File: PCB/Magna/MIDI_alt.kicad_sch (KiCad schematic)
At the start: 32 parts, among them J501 DIN-5_180degree, J502 DIN-5_180degree, J503 DIN-5_180degree, U501 74LVC2G14, U502 74LVC2G14, U503 74HC08D, U504 TLP2361

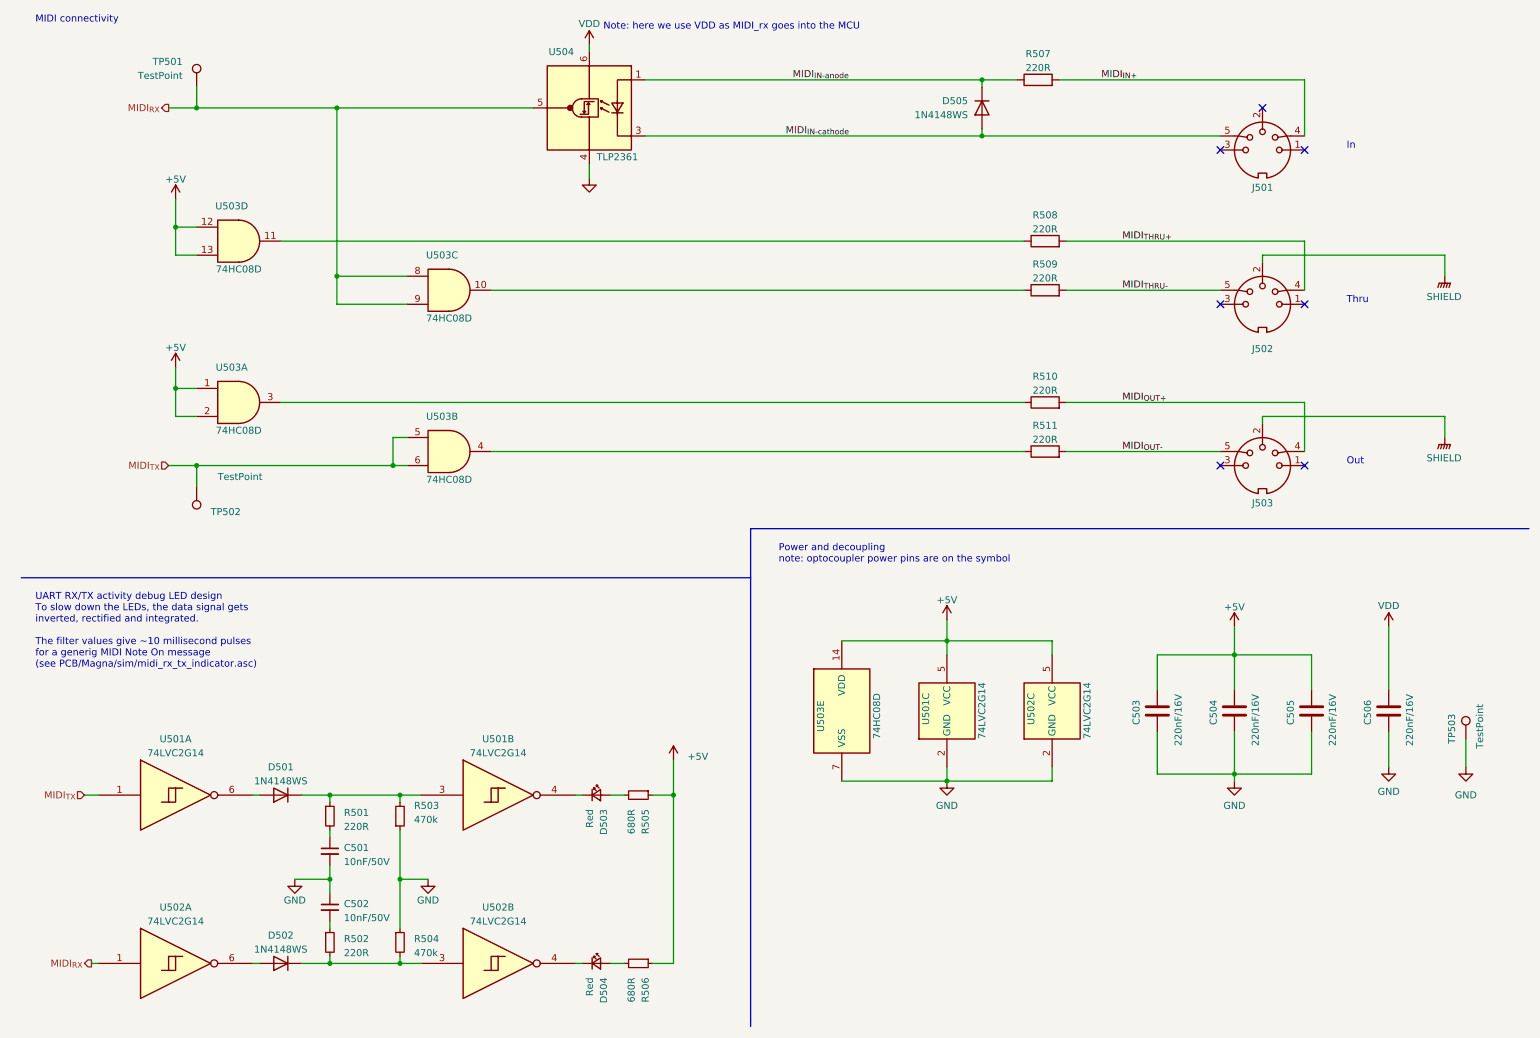
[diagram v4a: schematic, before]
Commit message: Update schematics to Kicad 9
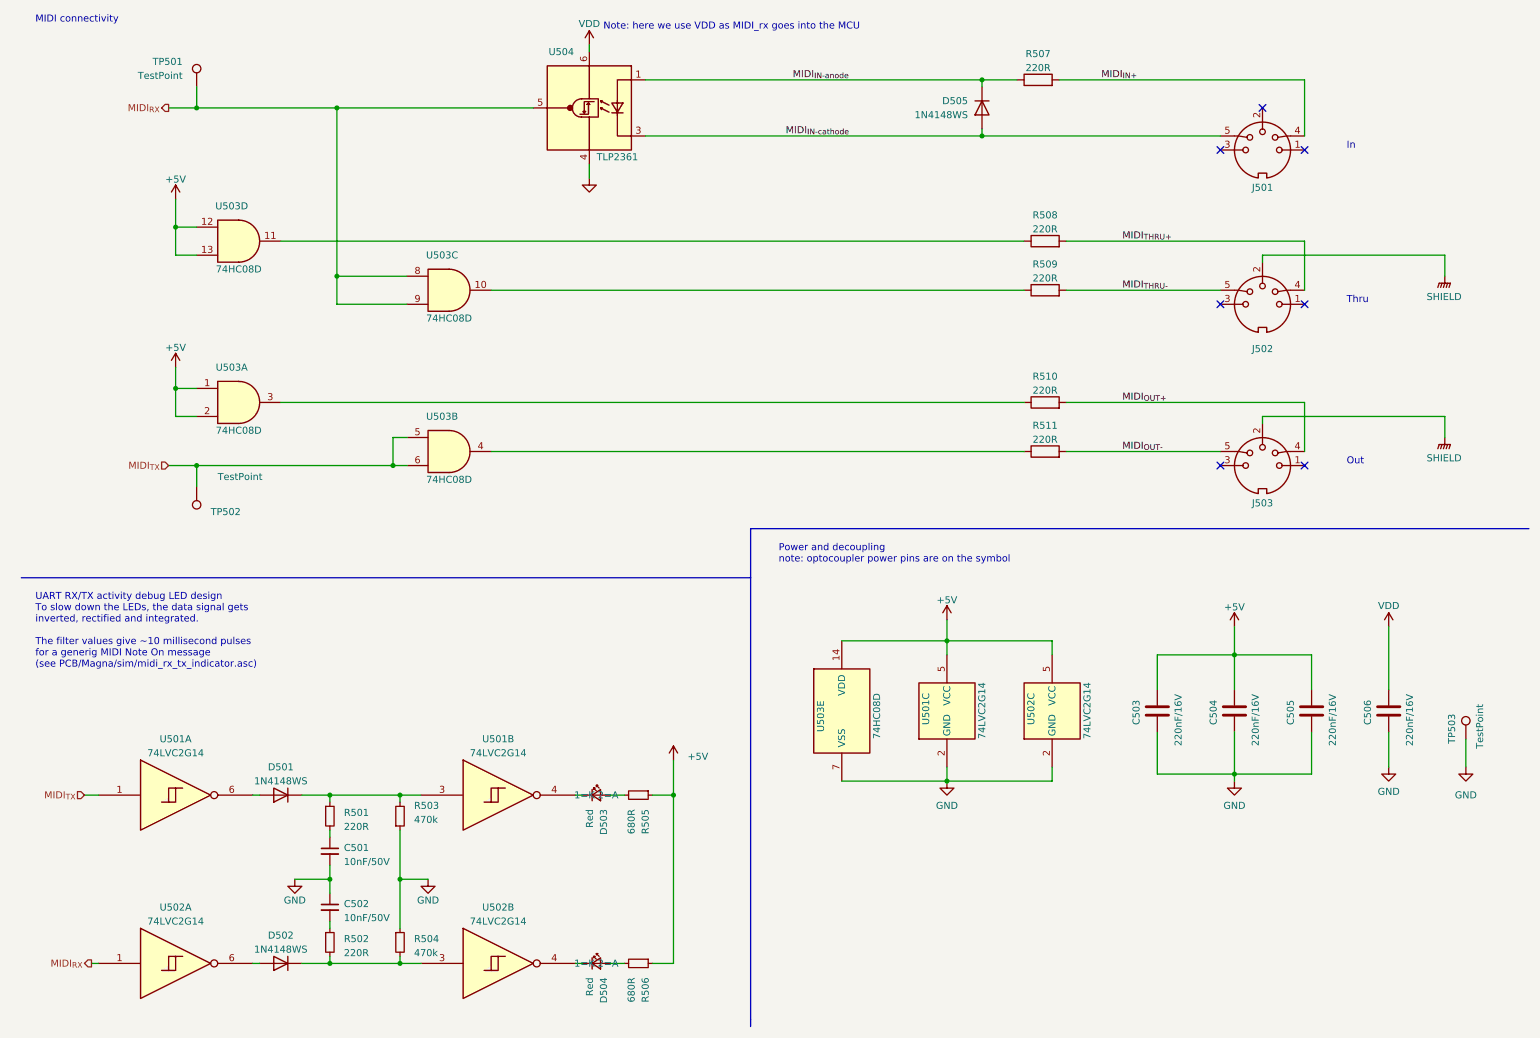
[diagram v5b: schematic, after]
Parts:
- D501, D502, D505: footprint Diode_SMD:D_SOD-123 -> Diode_SMD:D_SOD-523
- U504: footprint Package_SO:SO-5_4.4x3.6mm_P1.27mm -> Package_SO:SO-6L_10x3.84mm_P1.27mm
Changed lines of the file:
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@@
 (kicad_sch
-	(version 20231120)
+	(version 20250114)
 	(generator "eeschema")
-	(generator_version "8.0")
+	(generator_version "9.0")
 	(paper "A4")
+	(text "Power and decoupling\nnote: optocoupler power pins are on the symbol"
+		(exclude_from_sim no)
+		(at 149.86 114.3 0)
+		(effects
+			(font
+				(size 1.27 1.27)
+			)
+			(justify left bottom)
+		)
+	)
+	(text "Note: here we use VDD as MIDI_rx goes into the MCU"
+		(exclude_from_sim no)
+		(at 118.11 17.78 0)
+		(effects
+			(font
+				(size 1.27 1.27)
+			)
+			(justify left bottom)
+		)
+	)
+	(text "Out"
+		(exclude_from_sim no)
+		(at 252.73 96.52 0)
+		(effects
+			(font
+				(size 1.27 1.27)
+			)
+			(justify left bottom)
+		)
+	)
+	(text "MIDI connectivity"
+		(exclude_from_sim no)
+		(at 15.24 16.51 0)
+		(effects
+			(font
+				(size 1.27 1.27)
+			)
+			(justify left bottom)
+		)
+	)
+	(text "UART RX/TX activity debug LED design\nTo slow down the LEDs, the data signal gets \ninverted, rectified and integrated.\n\nThe filter values give ~10 millisecond pulses \nfor a generig MIDI Note On message \n(see PCB/Magna/sim/midi_rx_tx_indicator.asc)"
+		(exclude_from_sim no)
+		(at 15.24 133.35 0)
+		(effects
+			(font
+				(size 1.27 1.27)
+			)
+			(justify left bottom)
+		)
+	)
+	(text "Thru"
+		(exclude_from_sim no)
+		(at 252.73 67.31 0)
+		(effects
+			(font
+				(size 1.27 1.27)
+			)
+			(justify left bottom)
+		)
+	)
+	(text "In"
+		(exclude_from_sim no)
+		(at 252.73 39.37 0)
+		(effects
+			(font
+				(size 1.27 1.27)
+			)
+			(justify left bottom)
+		)
+	)
 	(junction
 		(at 186.69 26.67)
@@
 		)
 	)
-	(text "Power and decoupling\nnote: optocoupler power pins are on the symbol"
-		(exclude_from_sim no)
-		(at 149.86 114.3 0)
-		(effects
-			(font
-				(size 1.27 1.27)
-			)
-			(justify left bottom)
-		)
-	)
-	(text "Note: here we use VDD as MIDI_rx goes into the MCU"
-		(exclude_from_sim no)
-		(at 118.11 17.78 0)
-		(effects
-			(font
-				(size 1.27 1.27)
-			)
-			(justify left bottom)
-		)
-	)
-	(text "Out"
-		(exclude_from_sim no)
-		(at 252.73 96.52 0)
-		(effects
-			(font
-				(size 1.27 1.27)
-			)
-			(justify left bottom)
-		)
-	)
-	(text "MIDI connectivity"
-		(exclude_from_sim no)
-		(at 15.24 16.51 0)
-		(effects
-			(font
-				(size 1.27 1.27)
-			)
-			(justify left bottom)
-		)
-	)
-	(text "UART RX/TX activity debug LED design\nTo slow down the LEDs, the data signal gets \ninverted, rectified and integrated.\n\nThe filter values give ~10 millisecond pulses \nfor a generig MIDI Note On message \n(see PCB/Magna/sim/midi_rx_tx_indicator.asc)"
-		(exclude_from_sim no)
-		(at 15.24 133.35 0)
-		(effects
-			(font
-				(size 1.27 1.27)
-			)
-			(justify left bottom)
-		)
-	)
-	(text "Thru"
-		(exclude_from_sim no)
-		(at 252.73 67.31 0)
-		(effects
-			(font
-				(size 1.27 1.27)
-			)
-			(justify left bottom)
-		)
-	)
-	(text "In"
-		(exclude_from_sim no)
-		(at 252.73 39.37 0)
-		(effects
-			(font
-				(size 1.27 1.27)
-			)
-			(justify left bottom)
-		)
-	)
 	(label "MIDI_{OUT-}"
 		(at 212.09 93.98 0)
-		(fields_autoplaced yes)
 		(effects
 			(font
@@
 	(label "MIDI_{IN+}"
 		(at 208.28 26.67 0)
-		(fields_autoplaced yes)
 		(effects
 			(font
@@
 	(label "MIDI_{IN-cathode}"
 		(at 151.13 36.83 0)
-		(fields_autoplaced yes)
 		(effects
 			(font
@@
 	(label "MIDI_{IN-anode}"
 		(at 152.4 26.67 0)
-		(fields_autoplaced yes)
 		(effects
 			(font
@@
 	(label "MIDI_{THRU+}"
 		(at 212.09 55.88 0)
-		(fields_autoplaced yes)
 		(effects
 			(font
@@
 	(label "MIDI_{THRU-}"
 		(at 212.09 64.77 0)
-		(fields_autoplaced yes)
 		(effects
 			(font
@@
 	(label "MIDI_{OUT+}"
 		(at 212.09 85.09 0)
-		(fields_autoplaced yes)
 		(effects
 			(font
@@
 		(shape input)
 		(at 39.37 96.52 180)
-		(fields_autoplaced yes)
 		(effects
 			(font
@@
 		(shape output)
 		(at 39.37 31.75 180)
-		(fields_autoplaced yes)
 		(effects
 			(font
@@
 		(shape input)
 		(at 24.13 156.21 180)
-		(fields_autoplaced yes)
 		(effects
 			(font
@@
 		(shape output)
 		(at 25.4 186.69 180)
-		(fields_autoplaced yes)
 		(effects
 			(font
@@
 			)
 		)
-		(property "Footprint" "Diode_SMD:D_SOD-123"
+		(property "Footprint" "Diode_SMD:D_SOD-523"
 			(at 59.69 151.765 0)
 			(effects
@@
 	)
 	(symbol
-		(lib_id "SkrooterLib:SHIELD")
+		(lib_id "Skrooter_symbols:SHIELD")
 		(at 270.51 91.44 0)
 		(unit 1)
@@
 			)
 		)
+		(property "Sim.Pin" "1=K 2=A"
+			(at 116.84 156.21 0)
+			(effects
+				(font
+					(size 1.27 1.27)
+				)
+			)
+		)
 		(pin "1"
 		)
@@
 	)
 	(symbol
-		(lib_id "SkrooterLib:SHIELD")
+		(lib_id "Skrooter_symbols:SHIELD")
 		(at 270.51 62.23 0)
 		(unit 1)
@@
 			)
 		)
-		(property "Footprint" "Diode_SMD:D_SOD-123"
+		(property "Footprint" "Diode_SMD:D_SOD-523"
 			(at 59.69 182.245 0)
 			(effects
@@
 			)
 		)
-		(property "Footprint" "Package_SO:SO-5_4.4x3.6mm_P1.27mm"
+		(property "Footprint" "Package_SO:SO-6L_10x3.84mm_P1.27mm"
 			(at 156.21 21.59 0)
 			(effects
@@
 			)
 		)
-		(property "Footprint" "Diode_SMD:D_SOD-123"
+		(property "Footprint" "Diode_SMD:D_SOD-523"
 			(at 191.135 31.75 0)
 			(effects
@@
 			)
 		)
+		(property "Sim.Pin" "1=K 2=A"
+			(at 116.84 186.69 0)
+			(effects
+				(font
+					(size 1.27 1.27)
+				)
+			)
+		)

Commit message: Update Mainboard PCB
* Added better power ORing
* Added DRC for length matching
* Changed out components for cheaper production
* Removed some optional circuits from BOM for first prototype
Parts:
- J501, J502, J503, TP501, TP502, TP503: now left out of the parts list

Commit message: Update incorrect footprints on mainboard
For some reason footprints were incorrect on midi part.
Also 24.576MHz oscillator was incorrect.
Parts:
- D501, D502, D505: footprint Diode_SMD:D_SOD-523 -> Diode_SMD:D_SOD-123
- U504: footprint Package_SO:SO-6L_10x3.84mm_P1.27mm -> Package_SO:SO-5-6_4.55x3.7mm_P1.27mm
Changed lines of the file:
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@@
 			)
 		)
-		(property "Footprint" "Diode_SMD:D_SOD-523"
+		(property "Footprint" "Diode_SMD:D_SOD-123"
 			(at 59.69 151.765 0)
 			(effects
@@
 			)
 		)
-		(property "Footprint" "Diode_SMD:D_SOD-523"
+		(property "Footprint" "Diode_SMD:D_SOD-123"
 			(at 59.69 182.245 0)
 			(effects
@@
 			)
 		)
-		(property "Footprint" "Package_SO:SO-6L_10x3.84mm_P1.27mm"
+		(property "Footprint" "Package_SO:SO-5-6_4.55x3.7mm_P1.27mm"
 			(at 156.21 21.59 0)
 			(effects
@@
 			)
 		)
-		(property "Footprint" "Diode_SMD:D_SOD-523"
+		(property "Footprint" "Diode_SMD:D_SOD-123"
 			(at 191.135 31.75 0)
 			(effects
